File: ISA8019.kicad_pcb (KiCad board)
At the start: 2 copper layers, 104.1 x 71.9 mm, 54 parts, among them J1 Bus_ISA_8bit, J2 8P8C_Shielded, J4 Jumper mode, J5 PNP force, J6 BROM size and base address, J7 I/O base address, J8 Medium type, J9 IRQ Select, T1 13F-39MNL, U1 RTL8019AS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

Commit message: Add rev 2.2, supporting an 30SF040 EPROM, also additional address lines are now broken out
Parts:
- added J10: Extra Address Lines, Connector_PinHeader_2.54mm:PinHeader_1x03_P2.54mm_Vertical, F.Cu at (81.3, 73.0)
- U3: value SST39SF010 / MX29F001T -> SST39SF040
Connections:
- net /BS0 renamed /BA20
- net /BS1 renamed /BA19
- net /PNP renamed /BA21
- R11 pad 1: /BS2 -> /BA18
- R12 pad 1: /BS3 -> /BA17
- U1 pad 69: /BS2 -> /BA18
- U1 pad 71: /BS3 -> /BA17
- U3 pad 1: (no net) -> /BA18
- U3 pad 30: (no net) -> /BA17
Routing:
- net /BA21: track 22.1 -> 87.1 mm
- net /BA18: track 0.00 -> 55.3 mm
- net /BA17: track 0.00 -> 55.0 mm
- net /BS3: track 44.3 -> 0.00 mm
- net /BA19: track 30.0 -> 72.2 mm, vias 2 -> 3
- net /BS2: track 40.6 -> 0.00 mm
- net /BA20: track 35.6 -> 75.8 mm, vias 0 -> 1
- net GND: track 498.8 -> 517.6 mm, vias 12 -> 13
- net Earth: track 45.5 -> 51.5 mm, vias 0 -> 1
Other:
- board text added: "BA19"
- board text added: "BA20"
- board text added: "BA21"
- board text added: "RTL8019 ISA 8-Bit rev 2.2"
- board text removed: "RTL8019 ISA 8-Bit rev 2.1"

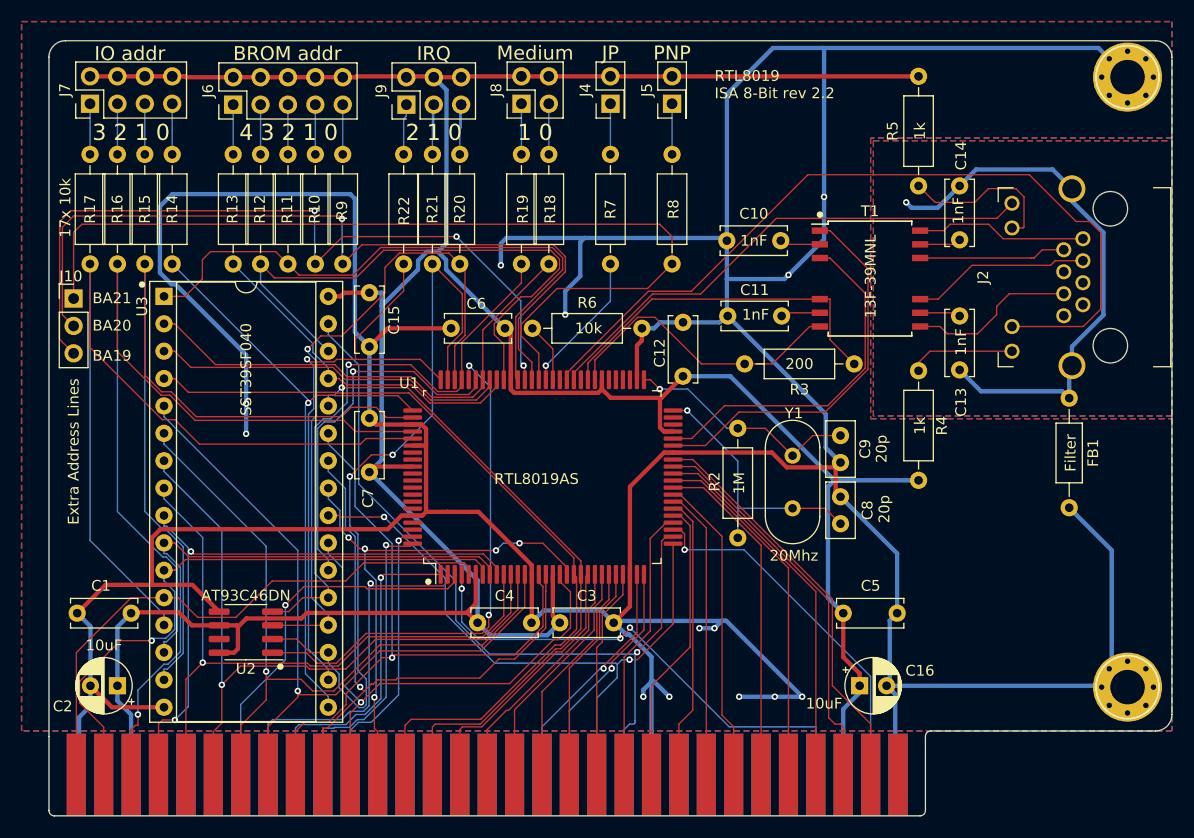
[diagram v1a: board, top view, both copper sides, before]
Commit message: Fix address BA14/16 ordering to SST39SF040
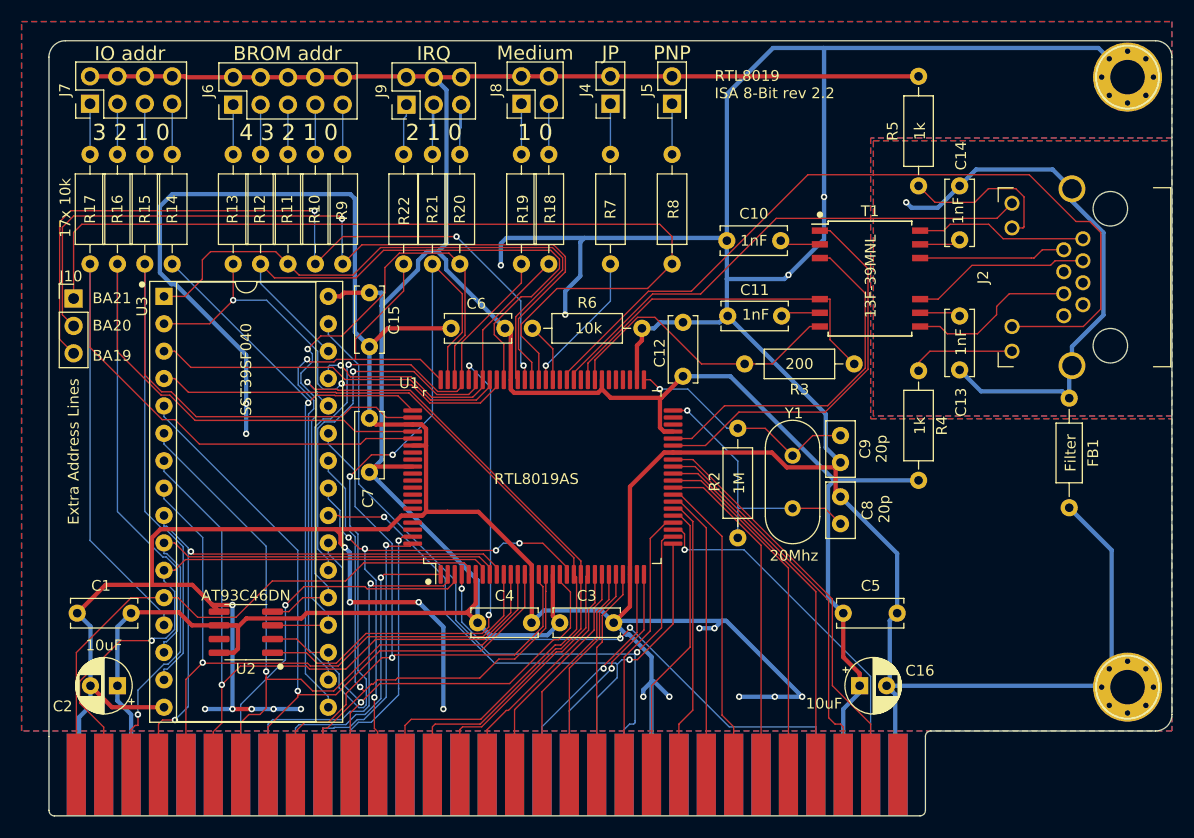
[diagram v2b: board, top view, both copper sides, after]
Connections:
- U3 pad 2: /BA14 -> /BA16
- U3 pad 29: /BA16 -> /BA14
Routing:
- net GND: track 517.6 -> 562.9 mm, vias 13 -> 23
- net /BA14: track 46.7 -> 31.2 mm, vias 0 -> 1
- net /BA16: track 32.1 -> 42.5 mm, vias 0 -> 2
- net /ISA_A13: track 59.6 -> 63.5 mm
- net /BD6: track 62.9 -> 63.8 mm
- net /ISA_A6: track 66.7 -> 67.4 mm
- net /BD4: track 55.0 -> 55.7 mm

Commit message: Add revision 2.3 of the board to jumper IRQ6 and 7 and keep them disconnected by default
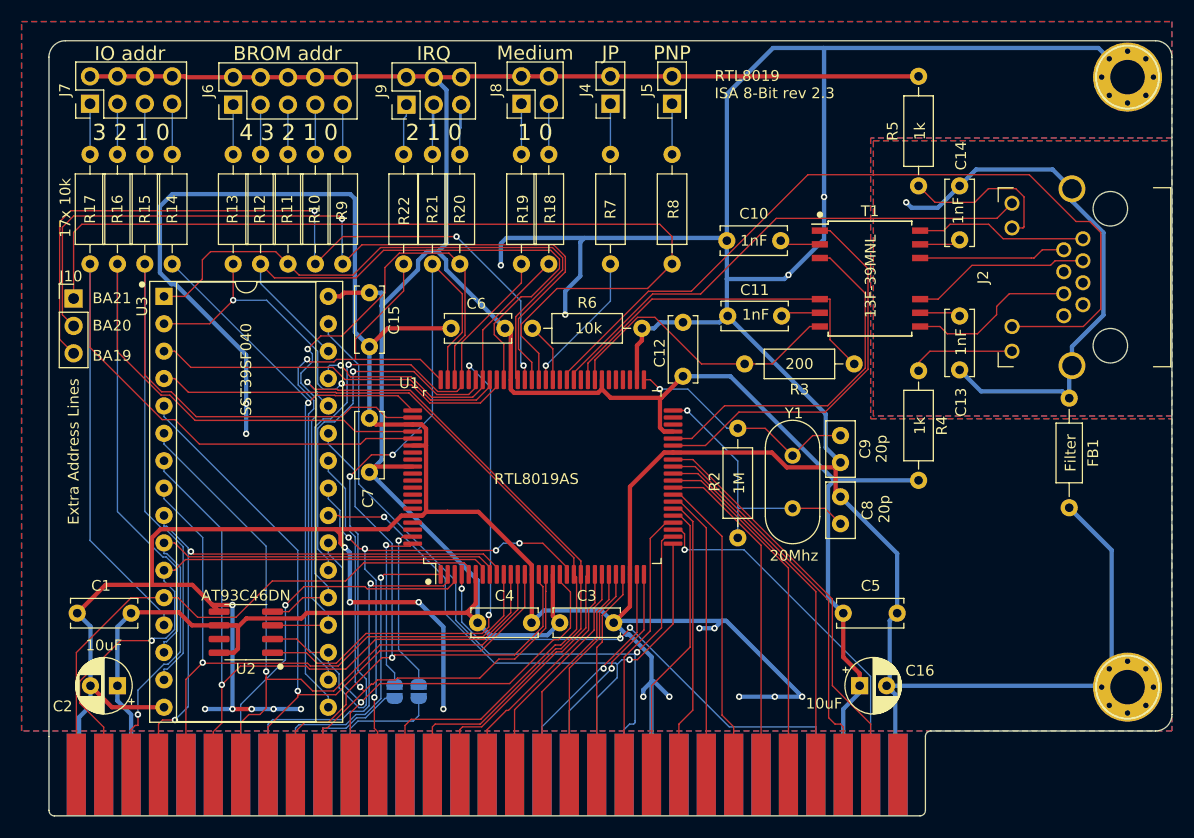
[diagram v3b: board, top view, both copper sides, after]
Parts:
- added JP1: IRQ6_Jumper, Jumper:SolderJumper-2_P1.3mm_Open_RoundedPad1.0x1.5mm, B.Cu at (111.1, 109.4)
- added JP2: IRQ6_Jumper, Jumper:SolderJumper-2_P1.3mm_Open_RoundedPad1.0x1.5mm, B.Cu at (113.3, 109.4)
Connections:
- net /~BCSB renamed /~{BCSB}
- net /~ISA_IOR renamed /~{ISA_IOR}
- net /~ISA_IOW renamed /~{ISA_IOW}
- net /~ISA_SMEMR renamed /~{ISA_SMEMR}
- net /~ISA_SMEMW renamed /~{ISA_SMEMW}
- J1 pad 15: (no net) -> unconnected-(J1-Pad15)
- J1 pad 16: (no net) -> unconnected-(J1-Pad16)
- J1 pad 17: (no net) -> unconnected-(J1-Pad17)
- J1 pad 18: (no net) -> unconnected-(J1-Pad18)
- J1 pad 19: (no net) -> unconnected-(J1-Pad19)
- J1 pad 20: (no net) -> unconnected-(J1-Pad20)
- J1 pad 26: (no net) -> unconnected-(J1-Pad26)
- J1 pad 27: (no net) -> unconnected-(J1-Pad27)
- J1 pad 28: (no net) -> unconnected-(J1-Pad28)
- J1 pad 30: (no net) -> unconnected-(J1-Pad30)
- J1 pad 32: (no net) -> unconnected-(J1-Pad32)
- J1 pad 5: (no net) -> unconnected-(J1-Pad5)
- J1 pad 6: (no net) -> unconnected-(J1-Pad6)
- J1 pad 7: (no net) -> unconnected-(J1-Pad7)
- J1 pad 8: (no net) -> unconnected-(J1-Pad8)
- J1 pad 9: (no net) -> +12V
- J2 pad 4: (no net) -> unconnected-(J2-Pad4)
- J2 pad 5: (no net) -> unconnected-(J2-Pad5)
- J2 pad 7: (no net) -> unconnected-(J2-Pad7)
- J2 pad 8: (no net) -> unconnected-(J2-Pad8)
- U1 pad 100: /ISA_IRQ6 -> Net-(JP1-Pad2)
- U1 pad 48: (no net) -> /TX-
- U1 pad 49: (no net) -> /TX+
- U1 pad 53: (no net) -> /CD-
- U1 pad 54: (no net) -> /CD+
- U1 pad 55: (no net) -> /RX-
- U1 pad 56: (no net) -> /RX+
- U1 pad 60: (no net) -> /LEDBNC
- U1 pad 63: (no net) -> /LED2
- U1 pad 87: (no net) -> /ISA_D15
- U1 pad 88: (no net) -> /ISA_D14
- U1 pad 90: (no net) -> /ISA_D13
- U1 pad 91: (no net) -> /ISA_D12
- U1 pad 92: (no net) -> /ISA_D11
- U1 pad 93: (no net) -> /ISA_D10
- U1 pad 94: (no net) -> /ISA_D9
- U1 pad 95: (no net) -> /ISA_D8
- U1 pad 97: (no net) -> unconnected-(U1-Pad97)
- U1 pad 98: (no net) -> unconnected-(U1-Pad98)
- U1 pad 99: /ISA_IRQ7 -> Net-(U1-Pad99)
- U2 pad 7: (no net) -> unconnected-(U2-Pad7)
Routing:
- net /ISA_IRQ6: track 28.1 -> 12.1 mm, vias 1 -> 0
- net Net-(JP1-Pad2): track 0.00 -> 15.9 mm, vias 0 -> 1
- net Net-(U1-Pad99): track 0.00 -> 15.6 mm, vias 0 -> 1
- net /ISA_IRQ7: track 25.8 -> 12.7 mm, vias 1 -> 0
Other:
- net class Default removed
- net class POWER removed
- board text added: "RTL8019 ISA 8-Bit rev 2.3"
- board text removed: "RTL8019 ISA 8-Bit rev 2.2"

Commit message: Prepare what will be revision 2.4
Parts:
- added J11: EPROM/SRAM Selection, Connector_PinHeader_2.54mm:PinHeader_2x03_P2.54mm_Vertical, F.Cu at (81.8, 83.9)
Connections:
- U3 pad 29: /BA14 -> /EPROM_A14
- U3 pad 31: /~{ISA_SMEMW} -> /EPROM_PGM
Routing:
- net /BA14: track 31.2 -> 76.0 mm, vias 1 -> 3
- net /EPROM_A14: track 0.00 -> 33.7 mm, vias 0 -> 2
- net /EPROM_PGM: track 0.00 -> 32.7 mm, vias 0 -> 2
- net GND: track 562.9 -> 580.1 mm, vias 23 -> 26
- net /~{ISA_SMEMW}: track 74.9 -> 86.6 mm, vias 1 -> 2
- net /BD0: track 77.9 -> 80.9 mm
- net /BD1: track 77.7 -> 78.3 mm
- net Earth: track 51.5 -> 52.0 mm
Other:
- board text added: "EPROM 1-3,4-6 SRAM 3-5,2-4"
- board text added: "RTL8019 ISA 8-Bit rev 2.4"
- board text removed: "RTL8019 ISA 8-Bit rev 2.3"

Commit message: Add Revision 2.4
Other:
- board text added: "EPROM: 1-3,4-6 SRAM: 3-5,2-4"
- board text removed: "EPROM 1-3,4-6 SRAM 3-5,2-4"
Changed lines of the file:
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@@
       (drillshape 0)
       (scaleselection 1)
-      (outputdirectory "gerbers/Rev_2.3")
+      (outputdirectory "gerbers/Rev_2.4")
     )
   )
@@
     (effects (font (size 1 1) (thickness 0.15)))
   )
-  (gr_text "EPROM\n  1-3,4-6\nSRAM\n  3-5,2-4" (at 79.308 94.784) (layer "F.SilkS")
-    (effects (font (size 1 1) (thickness 0.25)) (justify left))
+  (gr_text "EPROM:\n  1-3,4-6\nSRAM:\n  3-5,2-4" (at 80.578 93.514) (layer "F.SilkS")
+    (effects (font (size 0.8 0.8) (thickness 0.15)) (justify left))
   )
   (gr_text "3 2 1 0" (at 86.674 57.573) (layer "F.SilkS")
